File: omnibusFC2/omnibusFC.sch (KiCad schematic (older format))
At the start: 116 parts, among them J1 Conn_03, J10 Conn_06, J11 Conn_06, J12 Conn03, J13 Conn03, J14 Conn03, J15 Conn03, J16 Conn_01x01, J17 Conn_01x01, J2 Con02, J3 Conn_01x01, J4 Conn_06, J5 Conn_04, J6 Con02, J7 Conn03, J8 Conn_03, J9 Con02, Q1 MMBT3904, Q2 MMBT3904, Q3 MMBT3904, SW1 SW_Push, U1 STM32F405RGT6, U10 Micro_SD_Card_Det, U11 INA139, U2 MP1593, U3 MPU-9250, U4 MIC5332-SSYMT-TR, U9 MS5611-01BA, Y1 Crystal

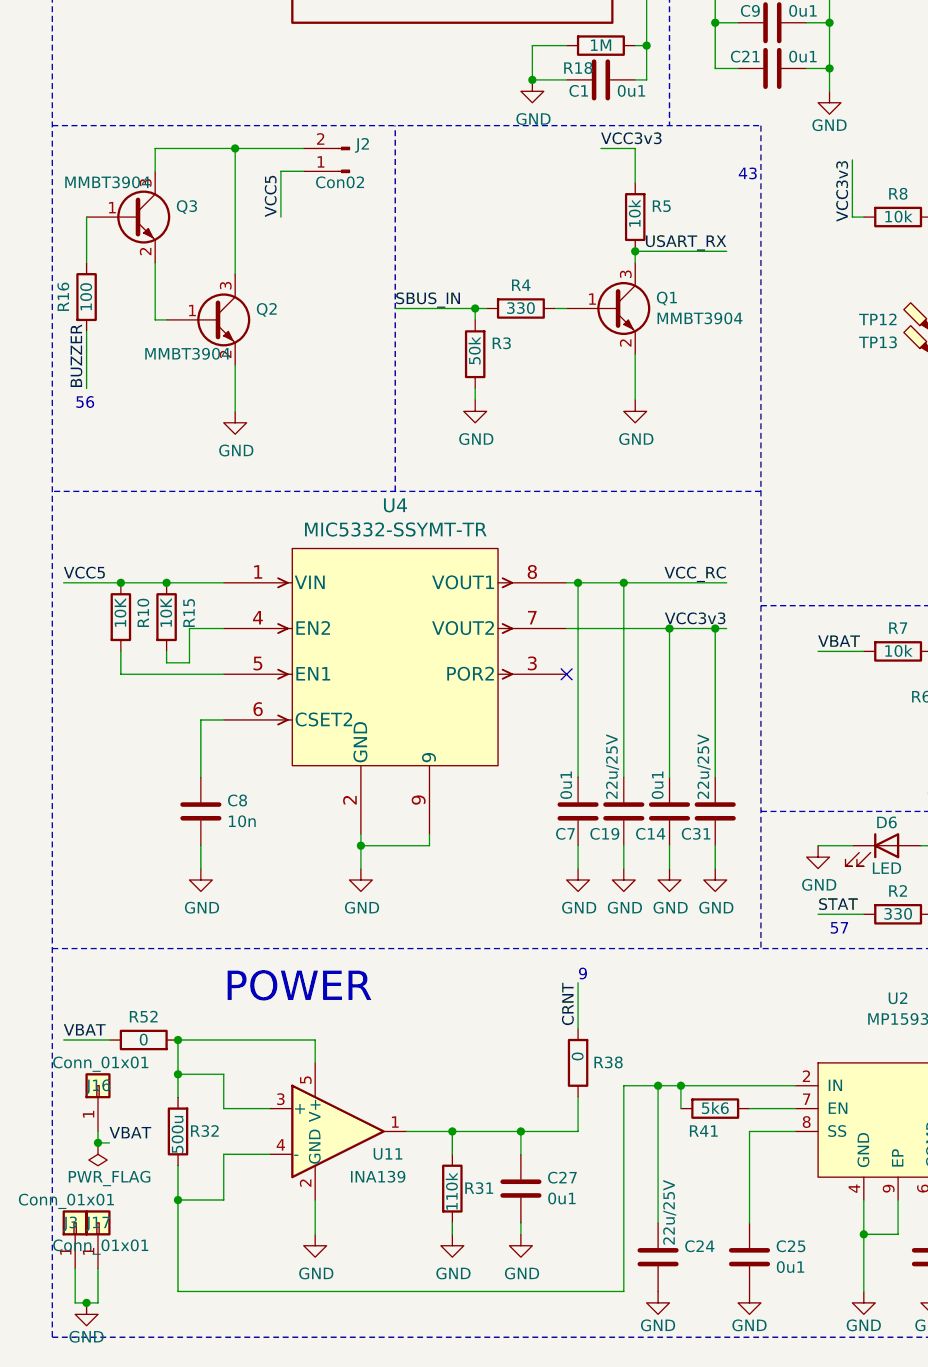
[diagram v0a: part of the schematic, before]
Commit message: 보드크기변경
그리기 어려워서 Multiwii_lite크기로 변경
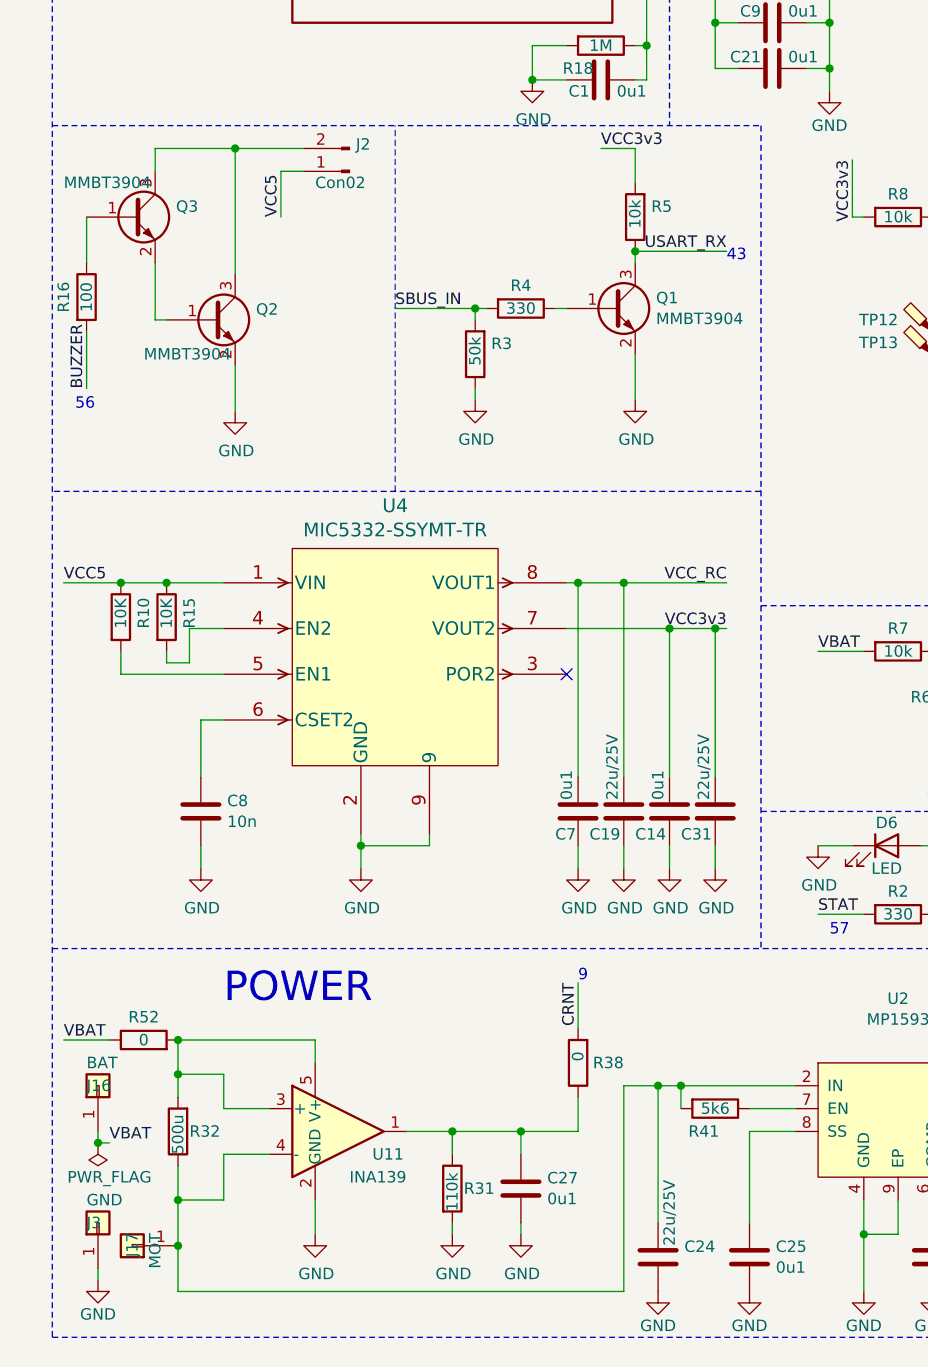
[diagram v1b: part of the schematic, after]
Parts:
- J16: value Conn_01x01 -> BAT
- J17: value Conn_01x01 -> MOT
- J3: value Conn_01x01 -> GND
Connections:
- net GND: no longer J17.1 (Pin_1)
- net at C24.1, R32.1, R41.2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: now also J17.1 (Pin_1)
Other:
- moved on the sheet: J17, J3
